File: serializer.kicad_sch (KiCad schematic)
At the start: 33 parts, among them U6 MAX9295A, Y1 Resonator_25MHz_ABM8G

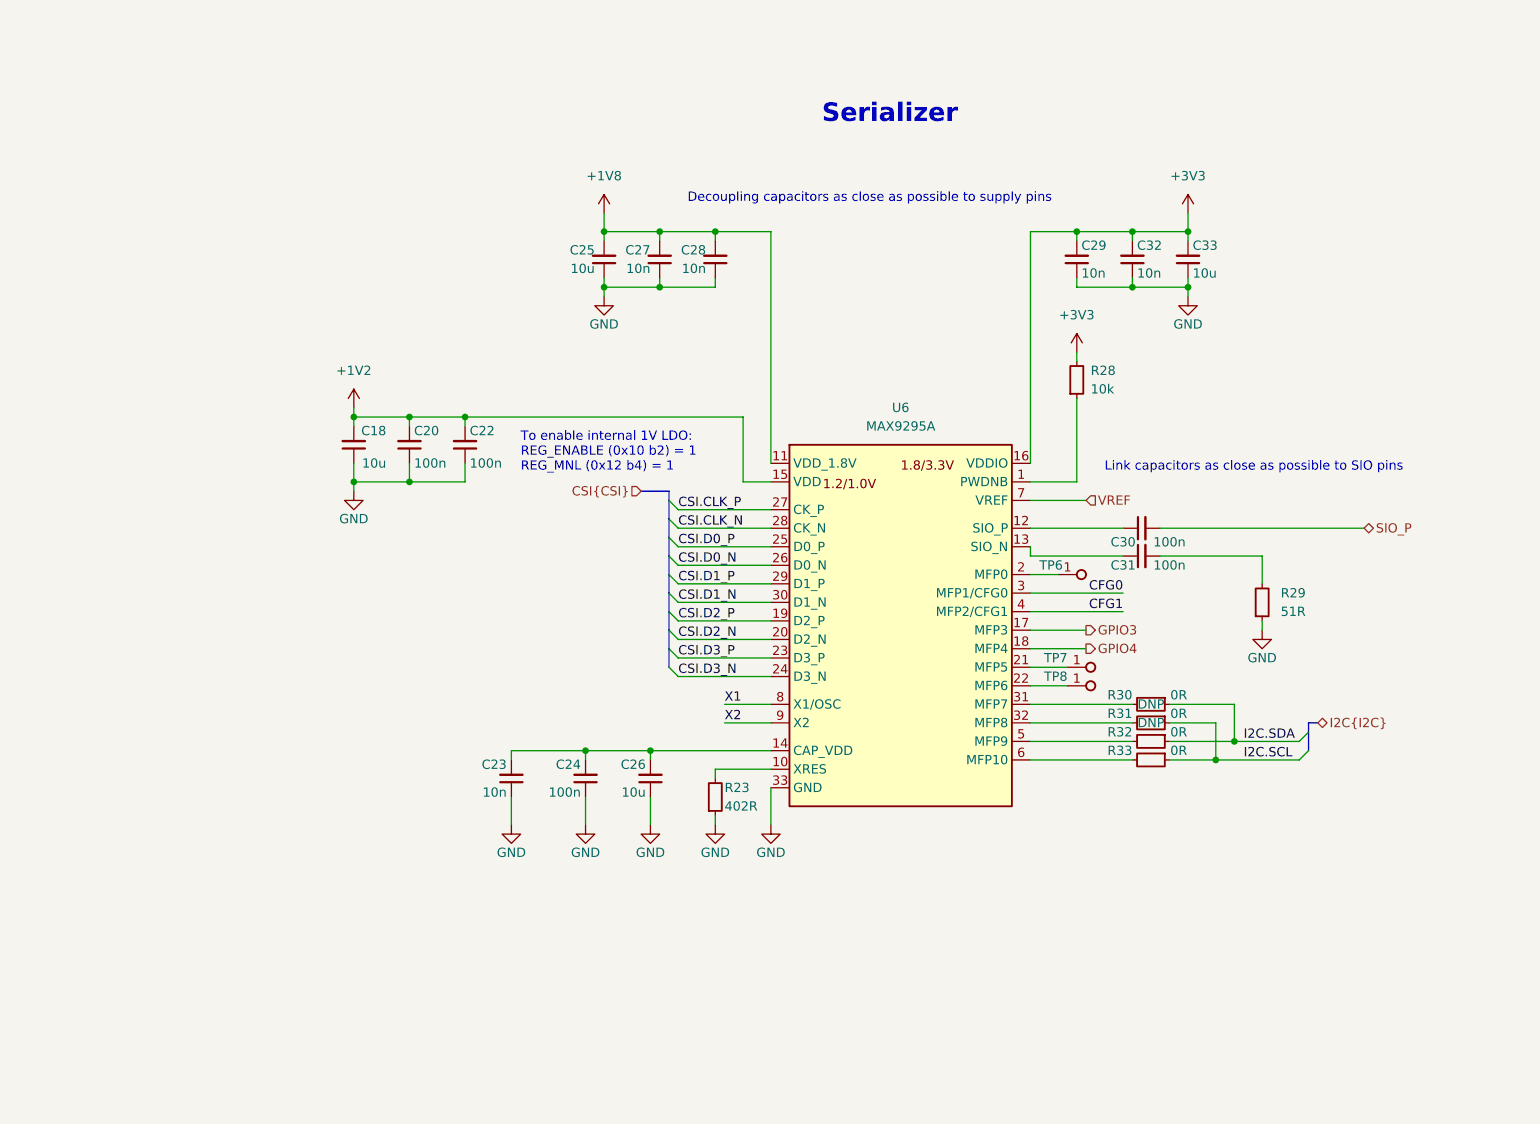
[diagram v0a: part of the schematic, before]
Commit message: [#66847] Serializer chip: MAX9295A -> MAX96717
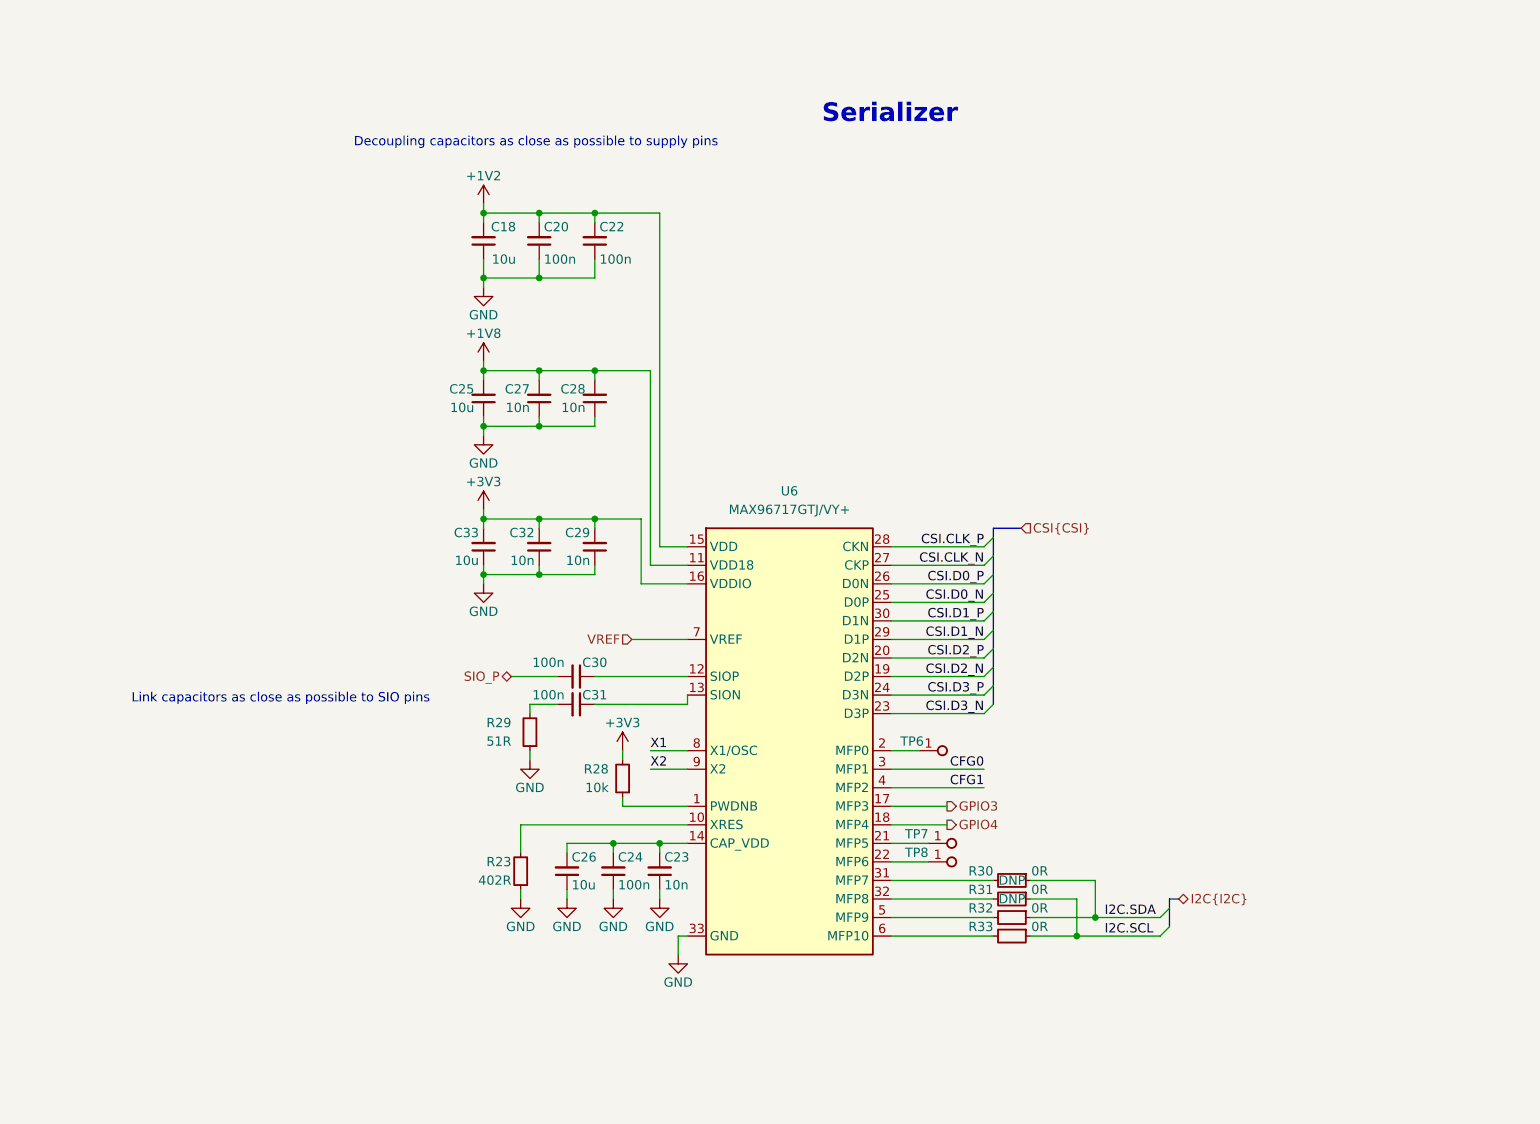
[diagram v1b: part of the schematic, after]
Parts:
- U6: value MAX9295A -> MAX96717GTJ_VY+; footprint antmicro-footprints:QFN-32-1EP_5x5mm -> antmicro-footprints:TQFN-32-1EP_5x5mm_P0.5mm; symbol antmicroInterfaceControllers:MAX9295A -> antmicroInterfaceControllers:MAX96717GTJ_VY+; MPN MAX9295A -> MAX96717GTJ/VY+; Manufacturer Maxim Integrated Products -> Analog Devices
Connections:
- net CSI.CLK_N: now also U6.27 (CKP); no longer U6.28 (CK_N)
- net CSI.CLK_P: now also U6.28 (CKN); no longer U6.27 (CK_P)
- net CSI.D0_N: now also U6.25 (D0P); no longer U6.26 (D0_N)
- net CSI.D0_P: now also U6.26 (D0N); no longer U6.25 (D0_P)
- net CSI.D1_N: now also U6.29 (D1P); no longer U6.30 (D1_N)
- net CSI.D1_P: now also U6.30 (D1N); no longer U6.29 (D1_P)
- net CSI.D2_N: now also U6.19 (D2P); no longer U6.20 (D2_N)
- net CSI.D2_P: now also U6.20 (D2N); no longer U6.19 (D2_P)
- net CSI.D3_N: now also U6.23 (D3P); no longer U6.24 (D3_N)
- net CSI.D3_P: now also U6.24 (D3N); no longer U6.23 (D3_P)
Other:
- note removed: "To enable internal 1V LDO: REG_ENABLE (0x10 b2) = 1 REG_MNL (0x12 b4) = 1"
- moved on the sheet: C18, C20, C22, C23, C24, C25, C26, C27, C28, C29, C30, C31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

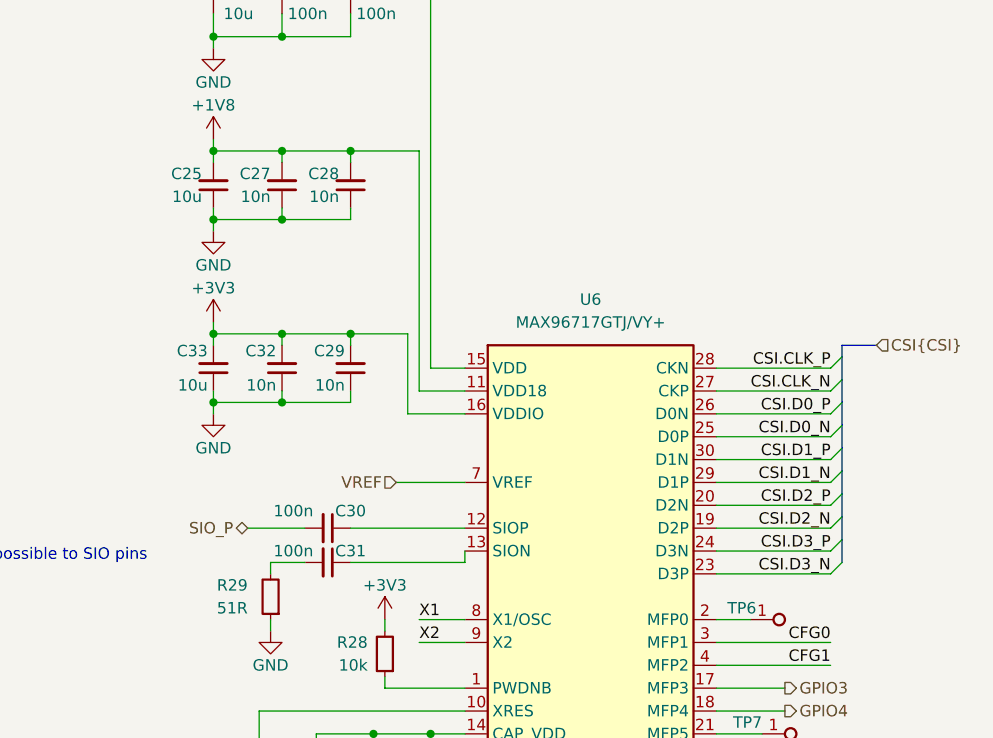
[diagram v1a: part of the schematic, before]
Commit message: [#66847] unDNP pullups on I2C; update pcb from sch
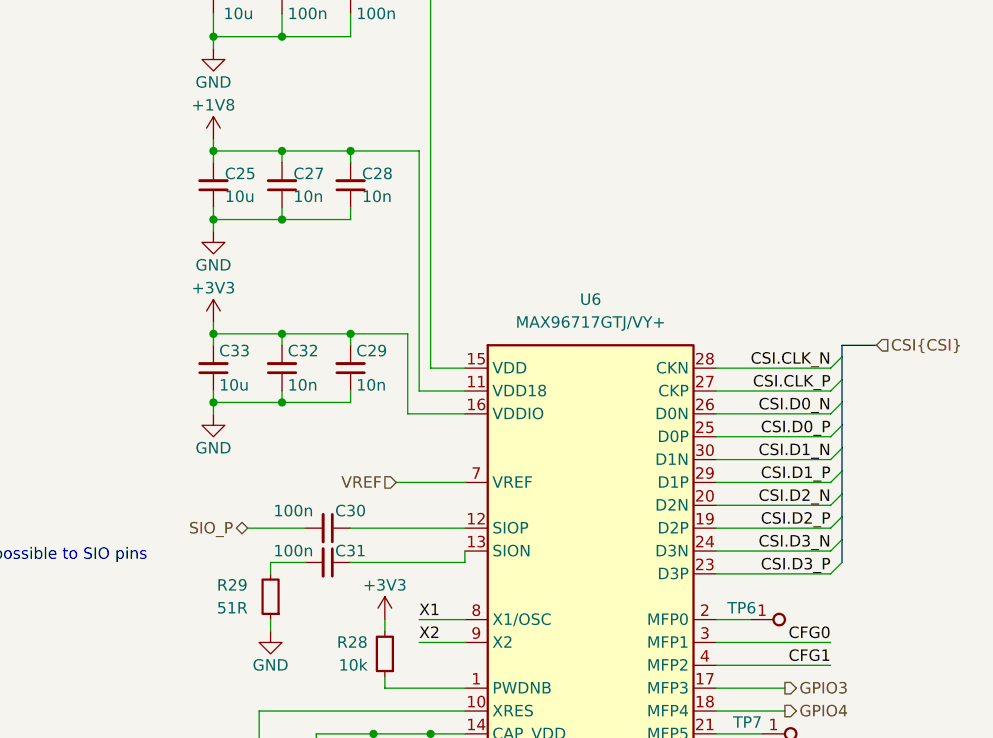
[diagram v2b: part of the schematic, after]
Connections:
- net CSI.CLK_N: now also U6.28 (CKN); no longer U6.27 (CKP)
- net CSI.CLK_P: now also U6.27 (CKP); no longer U6.28 (CKN)
- net CSI.D0_N: now also U6.26 (D0N); no longer U6.25 (D0P)
- net CSI.D0_P: now also U6.25 (D0P); no longer U6.26 (D0N)
- net CSI.D1_N: now also U6.30 (D1N); no longer U6.29 (D1P)
- net CSI.D1_P: now also U6.29 (D1P); no longer U6.30 (D1N)
- net CSI.D2_N: now also U6.20 (D2N); no longer U6.19 (D2P)
- net CSI.D2_P: now also U6.19 (D2P); no longer U6.20 (D2N)
- net CSI.D3_N: now also U6.24 (D3N); no longer U6.23 (D3P)
- net CSI.D3_P: now also U6.23 (D3P); no longer U6.24 (D3N)
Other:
- moved on the sheet: C25, C27, C28, C29, C32, C33

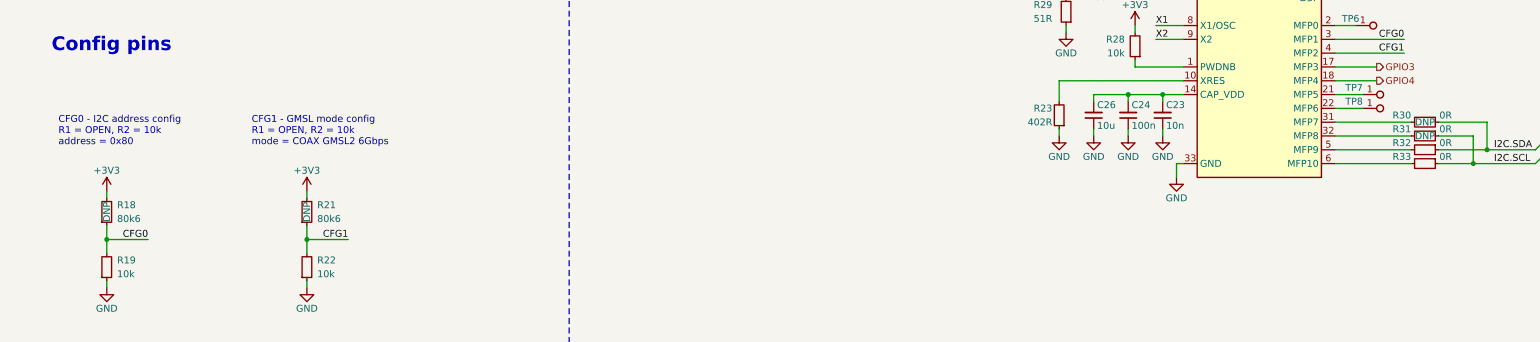
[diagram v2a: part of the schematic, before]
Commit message: [#66847] Update DNP style; Update from lib; Fix CSI bus definition
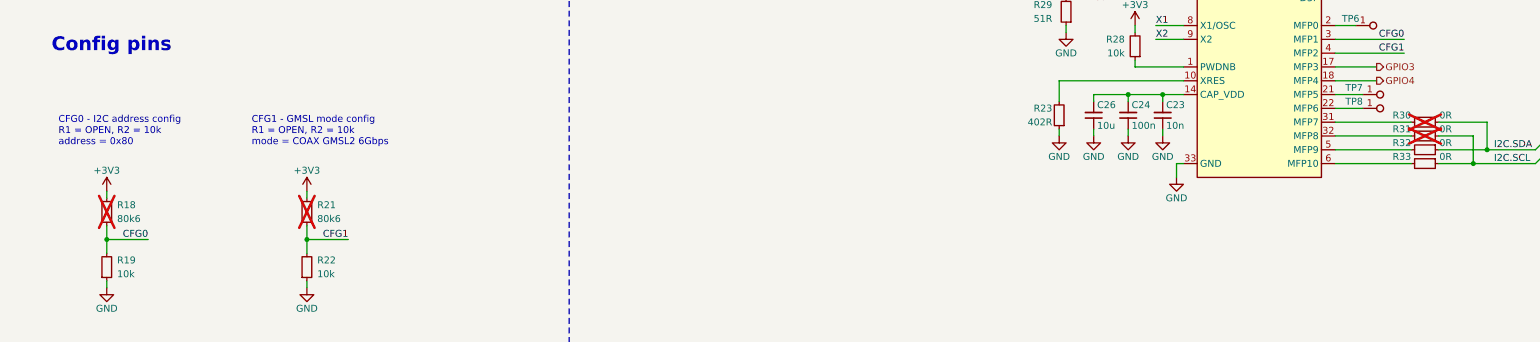
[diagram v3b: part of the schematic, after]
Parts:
- R18, R21, R30, R31: DNP DNP -> (none); now not fitted
- TP6, TP7, TP8: now left out of the parts list
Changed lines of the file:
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@@
     (comment 1 "www.antmicro.com")
   )
-  (bus_alias "CSI" (members "CLK_P" "D[0..3]_P" "D[0..3]_N" "CLK_N"))
+  (bus_alias "CSI" (members "CLK_P" "D0_P" "D0_N" "CLK_N" "D1_P" "D1_N" "D2_P" "D2_N" "D3_P" "D3_N"))
   (junction (at 223.52 140.97) (diameter 0) (color 0 0 0 0)
   )
@@
   )
   (symbol (lib_id "antmicroTestPoints:TP_1.5mm_SMD") (at 276.86 177.8 0) (unit 1)
-    (in_bom yes) (on_board yes) (dnp no)
+    (in_bom no) (on_board yes) (dnp no)
     (property "Reference" "TP7" (at 276.86 176.53 0)
       (effects (font (size 1.27 1.27) (thickness 0.15)) (justify right))
@@
   )
   (symbol (lib_id "antmicroTestPoints:TP_1.5mm_SMD") (at 276.86 180.34 0) (unit 1)
-    (in_bom yes) (on_board yes) (dnp no)
+    (in_bom no) (on_board yes) (dnp no)
     (property "Reference" "TP8" (at 276.86 179.07 0)
       (effects (font (size 1.27 1.27) (thickness 0.15)) (justify right))
@@
   )
   (symbol (lib_id "antmicroResistors0402:R_80k6_0402") (at 45.72 201.93 90) (unit 1)
-    (in_bom no) (on_board yes) (dnp no)
+    (in_bom no) (on_board yes) (dnp yes)
     (property "Reference" "R18" (at 47.625 198.12 90)
       (effects (font (size 1.27 1.27) (thickness 0.15)) (justify right))
@@
       (effects (font (size 1.27 1.27)) (justify left bottom) hide)
     )
-    (property "DNP" "DNP" (at 45.72 199.39 0)
-      (effects (font (size 1.27 1.27)))
-    )
     (pin "1")
     (pin "2")
@@
   )
   (symbol (lib_id "antmicroResistors0402:R_0R_0402") (at 290.83 182.88 0) (mirror y) (unit 1)
-    (in_bom no) (on_board yes) (dnp no)
+    (in_bom no) (on_board yes) (dnp yes)
     (property "Reference" "R30" (at 285.75 181.61 0)
       (effects (font (size 1.27 1.27) (thickness 0.15)) (justify left))
@@
       (effects (font (size 1.27 1.27) (thickness 0.15)) (justify left bottom) hide)
     )
-    (property "DNP" "DNP" (at 288.29 182.88 0)
-      (effects (font (size 1.27 1.27)))
-    )
     (pin "1")
     (pin "2")
@@
   )
   (symbol (lib_id "antmicroTestPoints:TP_1.5mm_SMD") (at 275.59 165.1 0) (unit 1)
-    (in_bom yes) (on_board yes) (dnp no)
+    (in_bom no) (on_board yes) (dnp no)
     (property "Reference" "TP6" (at 276.225 163.83 0)
       (effects (font (size 1.27 1.27) (thickness 0.15)) (justify right))
@@
   )
   (symbol (lib_id "antmicroResistors0402:R_0R_0402") (at 290.83 185.42 0) (mirror y) (unit 1)
-    (in_bom no) (on_board yes) (dnp no)
+    (in_bom no) (on_board yes) (dnp yes)
     (property "Reference" "R31" (at 285.75 184.15 0)
       (effects (font (size 1.27 1.27) (thickness 0.15)) (justify left))
@@
       (effects (font (size 1.27 1.27) (thickness 0.15)) (justify left bottom) hide)
     )
-    (property "DNP" "DNP" (at 288.29 185.42 0)
-      (effects (font (size 1.27 1.27)))
-    )
     (pin "1")
     (pin "2")
@@
   )
   (symbol (lib_id "antmicroResistors0402:R_80k6_0402") (at 82.55 201.93 90) (unit 1)
-    (in_bom no) (on_board yes) (dnp no)
+    (in_bom no) (on_board yes) (dnp yes)
     (property "Reference" "R21" (at 84.455 198.12 90)
       (effects (font (size 1.27 1.27) (thickness 0.15)) (justify right))
@@
       (effects (font (size 1.27 1.27)) (justify left bottom) hide)
     )
-    (property "DNP" "DNP" (at 82.55 199.39 0)
-      (effects (font (size 1.27 1.27)))
-    )
     (pin "1")

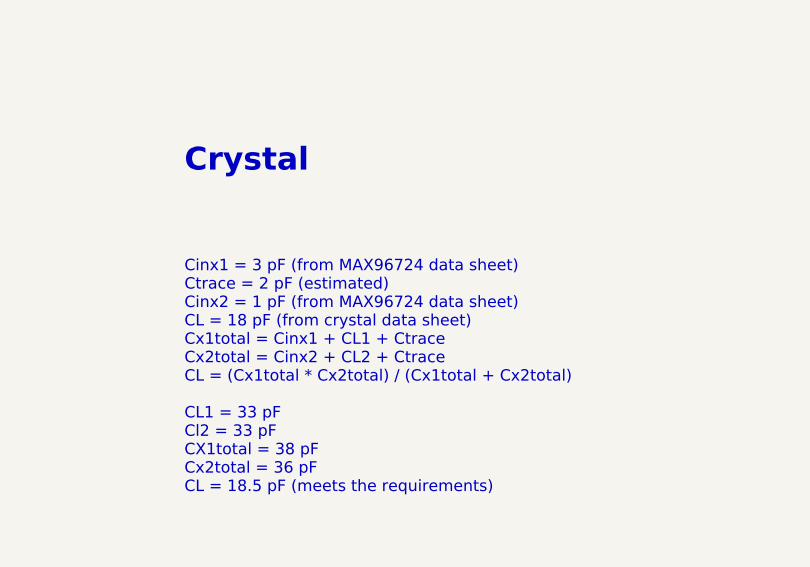
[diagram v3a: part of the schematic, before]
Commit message: [#66847] Bump date&rev; Clean ERC
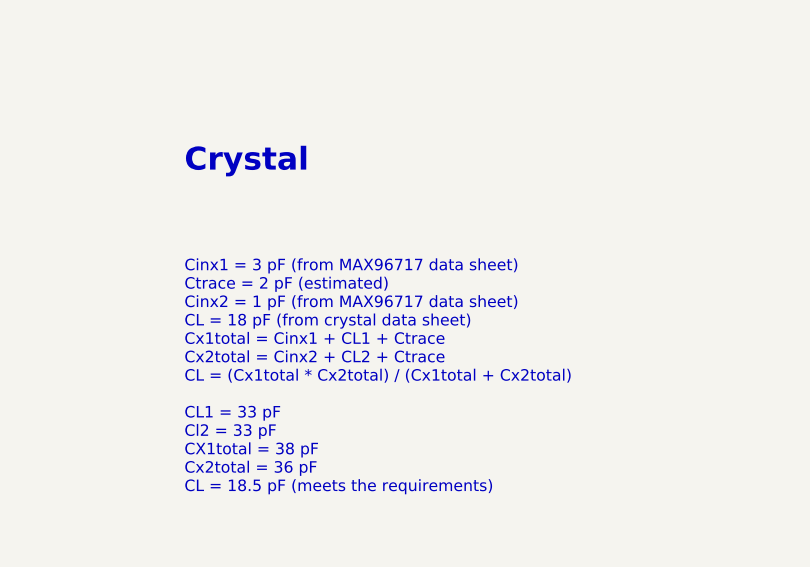
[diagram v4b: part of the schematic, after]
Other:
- note added: "Cinx1 = 3 pF (from MAX96717 data sheet) Ctrace = 2 pF (estimated) Cinx2 = 1 pF (from MAX96717 data sheet) CL = 18 pF (from crystal data sheet) Cx1total = Cinx1 + CL1 + Ctrace Cx2total = Cinx2 + CL2 + Ctrace CL = (Cx1total * Cx2total) / (Cx1total + Cx2total) CL1 = 33 pF Cl2 = 33 pF CX1total = 38 pF Cx2total = 36 pF CL = 18.5 pF (meets the requirements)"
- note removed: "Cinx1 = 3 pF (from MAX96724 data sheet) Ctrace = 2 pF (estimated) Cinx2 = 1 pF (from MAX96724 data sheet) CL = 18 pF (from crystal data sheet) Cx1total = Cinx1 + CL1 + Ctrace Cx2total = Cinx2 + CL2 + Ctrace CL = (Cx1total * Cx2total) / (Cx1total + Cx2total) CL1 = 33 pF Cl2 = 33 pF CX1total = 38 pF Cx2total = 36 pF CL = 18.5 pF (meets the requirements)"
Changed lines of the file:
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@@
   (title_block
     (title "GSML Serializer ")
-    (date "2024-06-19")
-    (rev "1.0.1")
+    (date "2024-10-08")
+    (rev "1.1.0")
     (company "Antmicro Ltd")
     (comment 1 "www.antmicro.com")
@@
     (effects (font (size 1.27 1.27)) (justify left bottom))
   )
-  (text "Cinx1 = 3 pF (from MAX96724 data sheet)\nCtrace = 2 pF (estimated)\nCinx2 = 1 pF (from MAX96724 data sheet)\nCL = 18 pF (from crystal data sheet)\nCx1total = Cinx1 + CL1 + Ctrace\nCx2total = Cinx2 + CL2 + Ctrace\nCL = (Cx1total * Cx2total) / (Cx1total + Cx2total)\n\nCL1 = 33 pF\nCl2 = 33 pF\nCX1total = 38 pF\nCx2total = 36 pF\nCL = 18.5 pF (meets the requirements)"
+  (text "Cinx1 = 3 pF (from MAX96717 data sheet)\nCtrace = 2 pF (estimated)\nCinx2 = 1 pF (from MAX96717 data sheet)\nCL = 18 pF (from crystal data sheet)\nCx1total = Cinx1 + CL1 + Ctrace\nCx2total = Cinx2 + CL2 + Ctrace\nCL = (Cx1total * Cx2total) / (Cx1total + Cx2total)\n\nCL1 = 33 pF\nCl2 = 33 pF\nCX1total = 38 pF\nCx2total = 36 pF\nCL = 18.5 pF (meets the requirements)"
     (at 40.64 76.2 0)
     (effects (font (size 1.27 1.27)) (justify left bottom))
